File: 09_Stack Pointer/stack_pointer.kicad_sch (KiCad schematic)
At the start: 37 parts, among them U1 74LS191, U2 74LS02, U3 74LS139, U4 74LS191, U5 74LS191

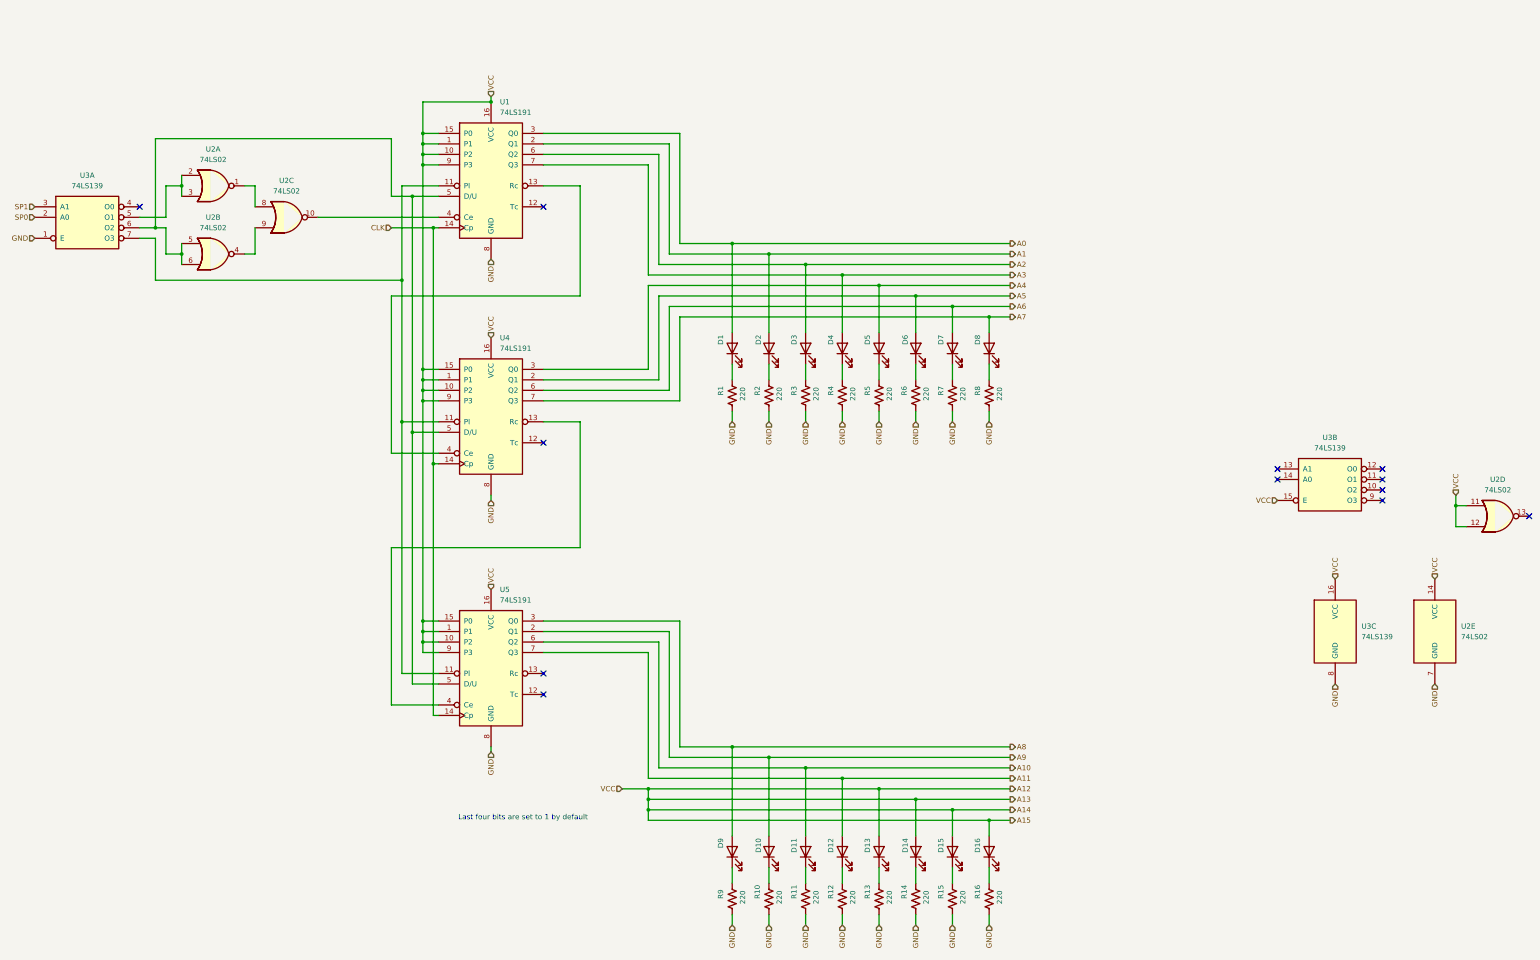
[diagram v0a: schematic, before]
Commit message: Last revision of the cpu, all boards have been ordered. Implementation to be tested and documented in following commits.
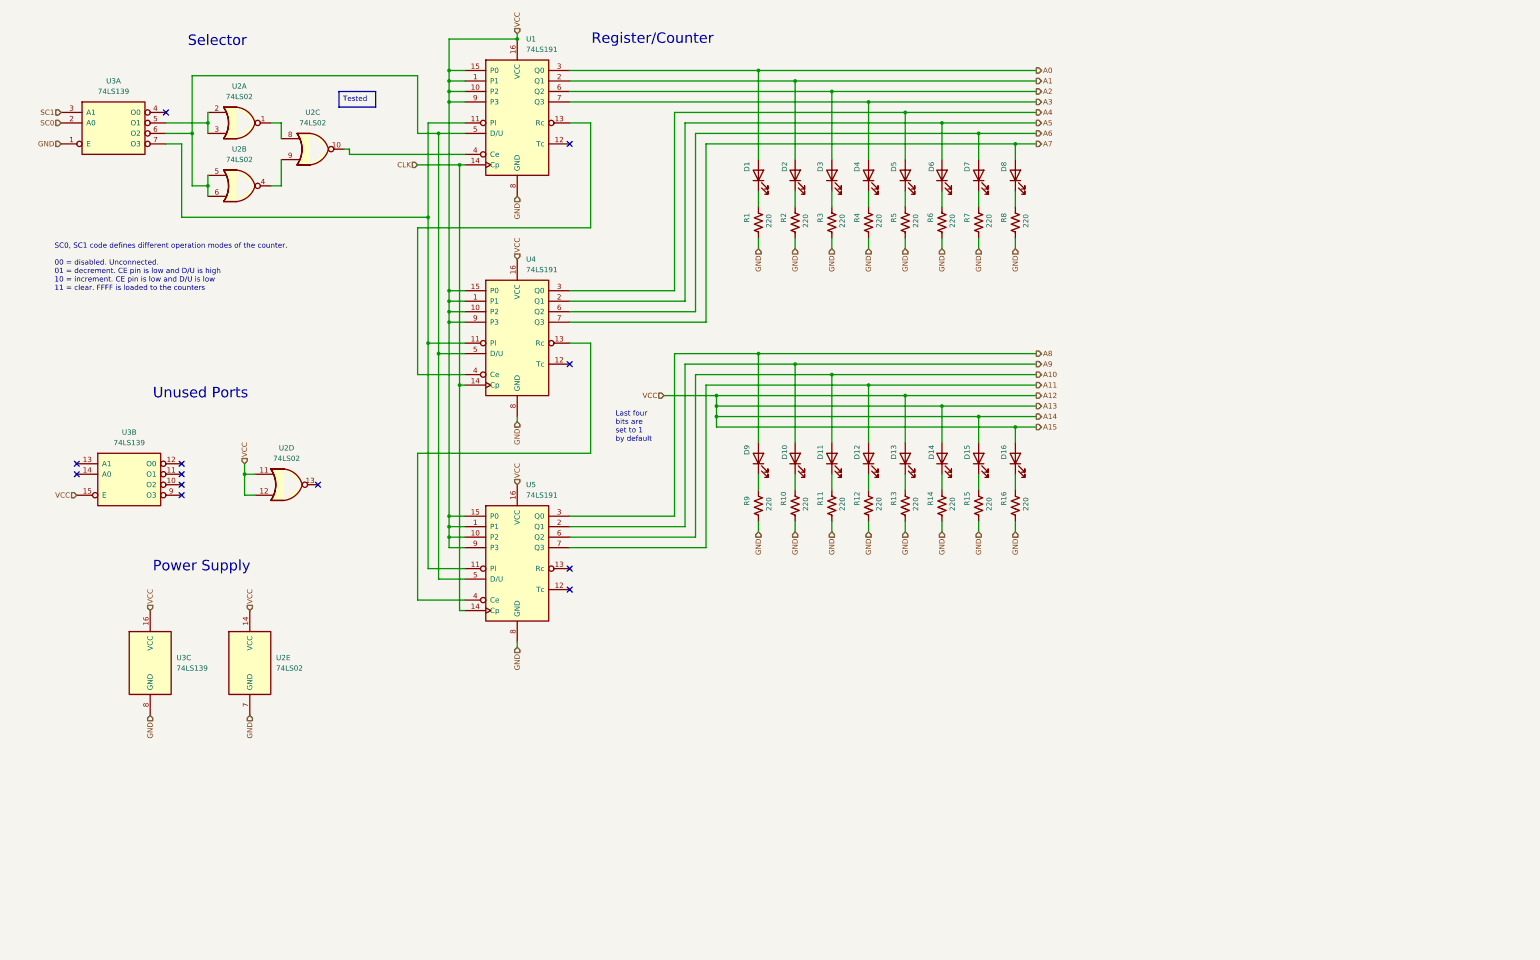
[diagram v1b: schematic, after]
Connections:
- net SP0 renamed SC0
- net SP1 renamed SC1
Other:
- note added: "Power Supply"
- note added: "Register/Counter"
- note added: "Selector"
- note added: "Unused Ports"
- moved on the sheet: D1, D10, D11, D12, D13, D14, D15, D16, D2, D3, D4, D5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
